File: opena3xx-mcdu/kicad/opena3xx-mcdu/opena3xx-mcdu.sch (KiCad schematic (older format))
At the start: 147 parts, among them J1 Conn_02x01, J2 Conn_02x01, J3 Conn_02x01, J4 Conn_02x01, J5 Conn_02x01, J6 Conn_02x01, J7 Conn_02x01, J8 Conn_02x01, SW1 TLL-6A, SW10 TLL-6A, SW100 SW_MEC_5E, SW11 TLL-6A, SW12 TLL-6A, SW13 TLL-6A, SW14 TLL-6A, SW15 TLL-6A, SW16 TLL-6A, SW17 TLL-6A, SW18 TLL-6A, SW19 TLL-6A, SW2 TLL-6A, SW20 TLL-6A, SW21 TLL-6A, SW22 TLL-6A, SW23 TLL-6A, SW24 TLL-6A, SW25 TLL-6A, SW26 TLL-6A, SW27 TLL-6A, SW28 TLL-6A, SW29 TLL-6A, SW3 TLL-6A, SW30 TLL-6A, SW31 TLL-6A, SW32 TLL-6A, SW33 TLL-6A, SW34 TLL-6A, SW35 TLL-6A, SW36 TLL-6A, SW37 TLL-6A, SW38 TLL-6A, SW39 TLL-6A, SW4 TLL-6A, SW40 TLL-6A, SW41 TLL-6A, SW42 TLL-6A, SW43 TLL-6A, SW44 TLL-6A, SW45 TLL-6A, SW46 TLL-6A, SW47 TLL-6A, SW48 TLL-6A, SW49 TLL-6A, SW5 TLL-6A, SW50 TLL-6A, SW51 TLL-6A, SW52 TLL-6A, SW53 TLL-6A, SW54 TLL-6A, SW55 TLL-6A, SW56 TLL-6A, SW57 TLL-6A, SW58 TLL-6A, SW59 TLL-6A, SW6 TLL-6A, SW60 TLL-6A, SW61 TLL-6A, SW62 TLL-6A, SW63 TLL-6A, SW64 TLL-6A, SW65 TLL-6A, SW66 TLL-6A, SW67 TLL-6A, SW68 TLL-6A, SW69 TLL-6A, SW7 TLL-6A, SW70 TLL-6A, SW71 TLL-6A, SW72 TLL-6A, SW73 TLL-6A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

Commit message: Added Libs + MCDU fixes + Added LCD Menu Tactile Switch
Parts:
- SW73: footprint openaa3xx:TACTILE_LED_TH -> opena3x:TACTILE_LED_TH
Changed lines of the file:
@@
 F 0 "SW73" H 18200 10830 50  0000 C CNN
 F 1 "TLL-6A" H 18200 10739 50  0000 C CNN
-F 2 "openaa3xx:TACTILE_LED_TH" H 18200 10648 50  0001 C CNN
+F 2 "opena3x:TACTILE_LED_TH" H 18200 10648 50  0001 C CNN
 F 3 "https://eu.mouser.com/datasheet/2/910/312_TL-6-1571269.pdf" H 18125 10675 50  0001 C CNN
 F 4 "DIM" H 18125 10625 50  0000 C CNN "MCDU IO Name"

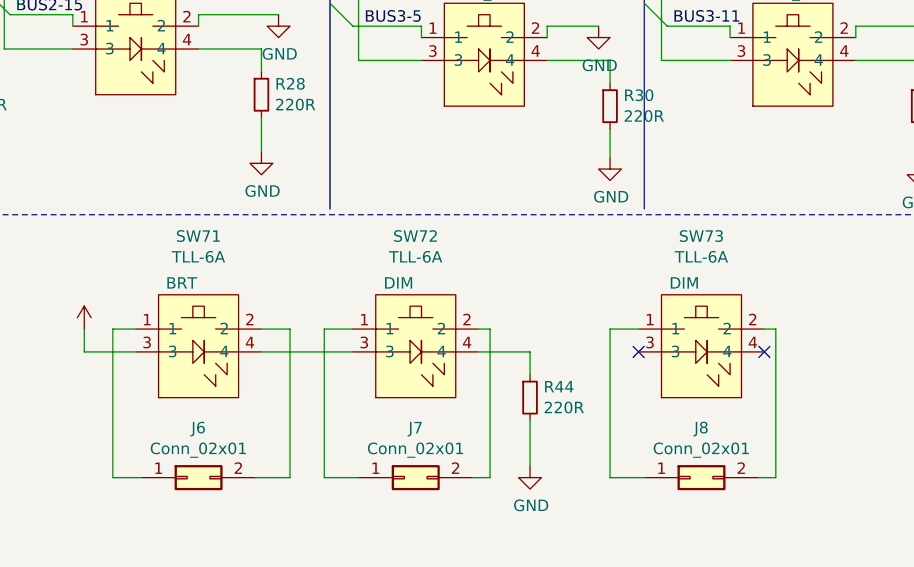
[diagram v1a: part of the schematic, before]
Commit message: Updates MCDU PCB
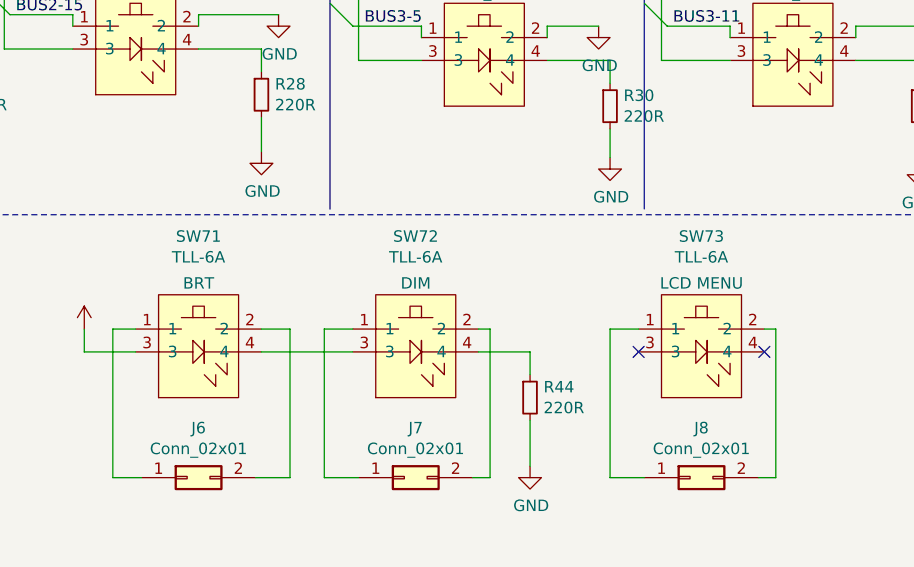
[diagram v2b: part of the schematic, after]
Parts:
- SW73: MCDU IO Name DIM -> LCD MENU
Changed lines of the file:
@@
 F 2 "openaa3xx:TACTILE_LED_TH" H 16000 10648 50  0001 C CNN
 F 3 "https://eu.mouser.com/datasheet/2/910/312_TL-6-1571269.pdf" H 15925 10675 50  0001 C CNN
-F 4 "BRT" H 15925 10625 50  0000 C CNN "MCDU IO Name"
+F 4 "BRT" H 16000 10625 50  0000 C CNN "MCDU IO Name"
 	1    15925 10625
 	1    0    0    -1
@@
 F 2 "openaa3xx:TACTILE_LED_TH" H 16950 10648 50  0001 C CNN
 F 3 "https://eu.mouser.com/datasheet/2/910/312_TL-6-1571269.pdf" H 16875 10675 50  0001 C CNN
-F 4 "DIM" H 16875 10625 50  0000 C CNN "MCDU IO Name"
+F 4 "DIM" H 16950 10625 50  0000 C CNN "MCDU IO Name"
 	1    16875 10625
 	1    0    0    -1
@@
 F 2 "opena3x:TACTILE_LED_TH" H 18200 10648 50  0001 C CNN
 F 3 "https://eu.mouser.com/datasheet/2/910/312_TL-6-1571269.pdf" H 18125 10675 50  0001 C CNN
-F 4 "DIM" H 18125 10625 50  0000 C CNN "MCDU IO Name"
+F 4 "LCD MENU" H 18200 10625 50  0000 C CNN "MCDU IO Name"
 	1    18125 10625
 	1    0    0    -1

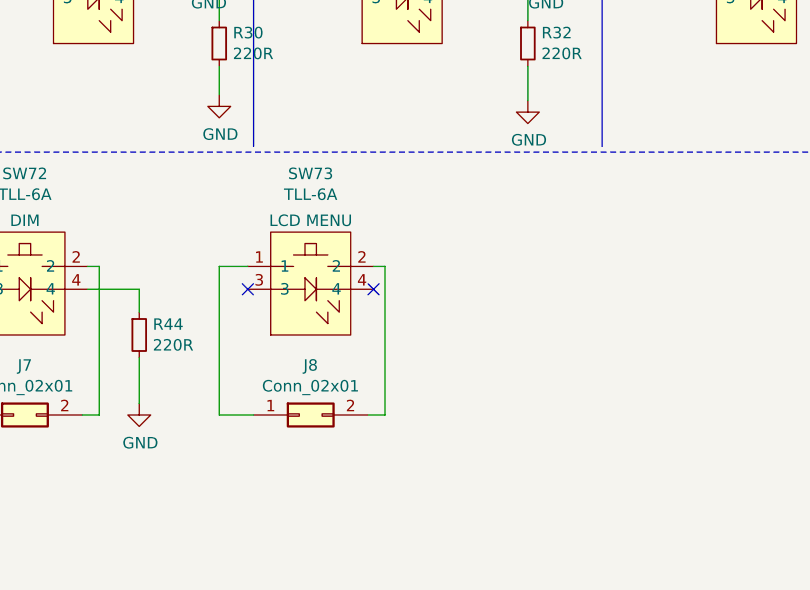
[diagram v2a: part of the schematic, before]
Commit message: MCDU Improvements Markings + Added Tactile for LCD Power + LED funcational names
MCDU Improvements Markings + Added Tactile for LCD Power + LED funcational names
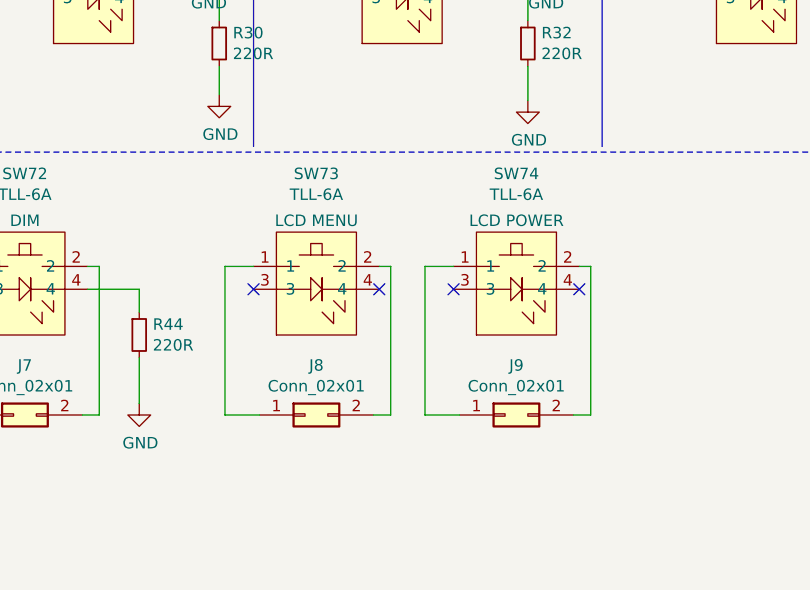
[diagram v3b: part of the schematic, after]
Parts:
- added J9: Conn_02x01, TerminalBlock:TerminalBlock_bornier-2_P5.08mm, symbol Connector_Generic:Conn_02x01
- added SW74: TLL-6A, opena3x:TACTILE_LED_TH, symbol opena3xx-mcdu-rescue:TLL-6A-opena3xx-kicad
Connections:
- new net: J9.1 (Pin_1), SW74.1
- new net: J9.2 (Pin_2), SW74.2
- no-connect marks 35 -> 37
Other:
- moved on the sheet: J8, SW73
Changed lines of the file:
@@
 L opena3xx-mcdu-rescue:TLL-6A-opena3xx-kicad SW73
 U 1 1 60CF5AE0
-P 18125 10625
-F 0 "SW73" H 18200 10830 50  0000 C CNN
-F 1 "TLL-6A" H 18200 10739 50  0000 C CNN
-F 2 "opena3x:TACTILE_LED_TH" H 18200 10648 50  0001 C CNN
-F 3 "https://eu.mouser.com/datasheet/2/910/312_TL-6-1571269.pdf" H 18125 10675 50  0001 C CNN
-F 4 "LCD MENU" H 18200 10625 50  0000 C CNN "MCDU IO Name"
-	1    18125 10625
+P 18150 10625
+F 0 "SW73" H 18225 10830 50  0000 C CNN
+F 1 "TLL-6A" H 18225 10739 50  0000 C CNN
+F 2 "opena3x:TACTILE_LED_TH" H 18225 10648 50  0001 C CNN
+F 3 "https://eu.mouser.com/datasheet/2/910/312_TL-6-1571269.pdf" H 18150 10675 50  0001 C CNN
+F 4 "LCD MENU" H 18225 10625 50  0000 C CNN "MCDU IO Name"
+	1    18150 10625
 	1    0    0    -1
 $EndComp
@@
 L Connector_Generic:Conn_02x01 J8
 U 1 1 60CF5AF6
-P 18150 11475
-F 0 "J8" H 18200 11692 50  0000 C CNN
-F 1 "Conn_02x01" H 18200 11601 50  0000 C CNN
-F 2 "TerminalBlock:TerminalBlock_bornier-2_P5.08mm" H 18150 11475 50  0001 C CNN
-F 3 "~" H 18150 11475 50  0001 C CNN
-	1    18150 11475
+P 18175 11475
+F 0 "J8" H 18225 11692 50  0000 C CNN
+F 1 "Conn_02x01" H 18225 11601 50  0000 C CNN
+F 2 "TerminalBlock:TerminalBlock_bornier-2_P5.08mm" H 18175 11475 50  0001 C CNN
+F 3 "~" H 18175 11475 50  0001 C CNN
+	1    18175 11475
 	1    0    0    -1
 $EndComp
 Wire Wire Line
-	17800 10825 17800 11475
+	17825 10825 17825 11475
 Wire Wire Line
-	17800 11475 17950 11475
+	17825 11475 17975 11475
 Wire Wire Line
-	18450 11475 18525 11475
+	18475 11475 18550 11475
 Wire Wire Line
-	18525 11475 18525 10825
+	18550 11475 18550 10825
 Wire Wire Line
-	18525 10825 18475 10825
+	18550 10825 18500 10825
 Wire Wire Line
-	17800 10825 17925 10825
-NoConn ~ 18475 10925
-NoConn ~ 17925 10925
+	17825 10825 17950 10825
+NoConn ~ 18500 10925
+NoConn ~ 17950 10925
+$Comp
+L opena3xx-mcdu-rescue:TLL-6A-opena3xx-kicad SW74
+U 1 1 60E35CFB
+P 19025 10625
+F 0 "SW74" H 19100 10830 50  0000 C CNN
+F 1 "TLL-6A" H 19100 10739 50  0000 C CNN
+F 2 "opena3x:TACTILE_LED_TH" H 19100 10648 50  0001 C CNN
+F 3 "https://eu.mouser.com/datasheet/2/910/312_TL-6-1571269.pdf" H 19025 10675 50  0001 C CNN
+F 4 "LCD POWER" H 19100 10625 50  0000 C CNN "MCDU IO Name"
+	1    19025 10625
+	1    0    0    -1
+$EndComp
+$Comp
+L Connector_Generic:Conn_02x01 J9
+U 1 1 60E35D01
+P 19050 11475
+F 0 "J9" H 19100 11692 50  0000 C CNN
+F 1 "Conn_02x01" H 19100 11601 50  0000 C CNN
+F 2 "TerminalBlock:TerminalBlock_bornier-2_P5.08mm" H 19050 11475 50  0001 C CNN
+F 3 "~" H 19050 11475 50  0001 C CNN
+	1    19050 11475
+	1    0    0    -1
+$EndComp
+Wire Wire Line
+	18700 10825 18700 11475
+Wire Wire Line
+	18700 11475 18850 11475
+Wire Wire Line
+	19350 11475 19425 11475
+Wire Wire Line
+	19425 11475 19425 10825
+Wire Wire Line
+	19425 10825 19375 10825
+Wire Wire Line
+	18700 10825 18825 10825
+NoConn ~ 19375 10925
+NoConn ~ 18825 10925
 Wire Bus Line
 	20850 5125 20850 10300

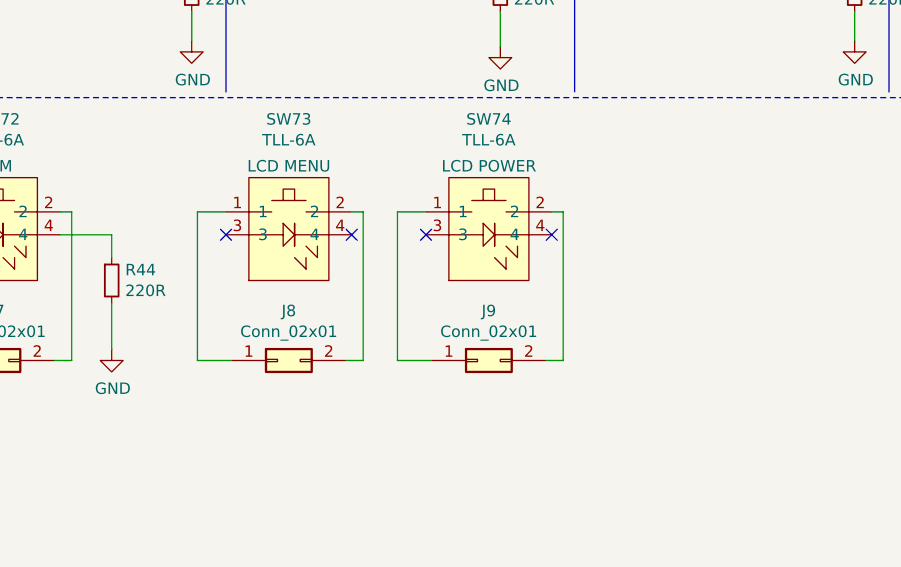
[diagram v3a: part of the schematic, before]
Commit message: PCB Update
1) 12V connecters moved up slightly to allow room for mounting nut.
2) Connected the LED's for the 'LCD MENU' and 'LCD PWR'.
3) Added 2 resistors for the 'LCD MENU' and 'LCD PWR' to allow direct connection to the display PCB.
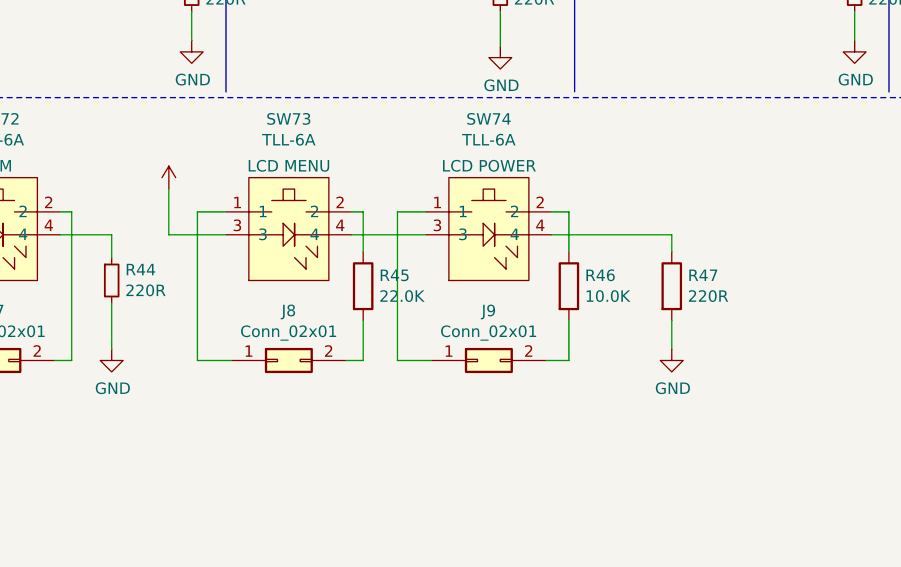
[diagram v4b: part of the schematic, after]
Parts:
- added R45: 22.0K, Resistor_SMD:R_1210_3225Metric_Pad1.30x2.65mm_HandSolder, symbol Device:R
- added R46: 10.0K, Resistor_SMD:R_1210_3225Metric_Pad1.30x2.65mm_HandSolder, symbol Device:R
- added R47: 220R, Resistor_SMD:R_1210_3225Metric_Pad1.30x2.65mm_HandSolder, symbol Device:R
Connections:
- net +12V: now also SW73.3
- net GND: now also R47.2
- net at SW73.2: now also R45.1; no longer J8.2 (Pin_2)
- net at SW73.4: now also SW74.3
- net at SW74.2: now also R46.1; no longer J9.2 (Pin_2)
- net at SW74.4: now also R47.1
- new net: J8.2 (Pin_2), R45.2
- new net: J9.2 (Pin_2), R46.2
- no-connect marks 37 -> 33
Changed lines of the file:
@@
 	18475 11475 18550 11475
 Wire Wire Line
-	18550 11475 18550 10825
+	18550 11475 18550 11300
 Wire Wire Line
 	18550 10825 18500 10825
 Wire Wire Line
 	17825 10825 17950 10825
-NoConn ~ 18500 10925
-NoConn ~ 17950 10925
 $Comp
 L opena3xx-mcdu-rescue:TLL-6A-opena3xx-kicad SW74
@@
 	18700 11475 18850 11475
 Wire Wire Line
-	19350 11475 19425 11475
+	18700 10825 18825 10825
+$Comp
+L Device:R R45
+U 1 1 61E2AB88
+P 18550 11150
+F 0 "R45" H 18620 11196 50  0000 L CNN
+F 1 "22.0K" H 18620 11105 50  0000 L CNN
+F 2 "Resistor_SMD:R_1210_3225Metric_Pad1.30x2.65mm_HandSolder" V 18480 11150 50  0001 C CNN
+F 3 "~" H 18550 11150 50  0001 C CNN
+	1    18550 11150
+	1    0    0    -1
+$EndComp
 Wire Wire Line
-	19425 11475 19425 10825
+	18550 11000 18550 10825
+$Comp
+L Device:R R46
+U 1 1 61E2B673
+P 19450 11150
+F 0 "R46" H 19520 11196 50  0000 L CNN
+F 1 "10.0K" H 19520 11105 50  0000 L CNN
+F 2 "Resistor_SMD:R_1210_3225Metric_Pad1.30x2.65mm_HandSolder" V 19380 11150 50  0001 C CNN
+F 3 "~" H 19450 11150 50  0001 C CNN
+	1    19450 11150
+	1    0    0    -1
+$EndComp
 Wire Wire Line
-	19425 10825 19375 10825
+	19350 11475 19450 11475
 Wire Wire Line
-	18700 10825 18825 10825
-NoConn ~ 19375 10925
-NoConn ~ 18825 10925
+	19450 11475 19450 11300
+Wire Wire Line
+	19450 10825 19450 11000
+Wire Wire Line
+	19375 10825 19450 10825
+Wire Wire Line
+	17950 10925 17700 10925
+Wire Wire Line
+	17700 10925 17700 10725
+Wire Wire Line
+	18500 10925 18825 10925
+Wire Wire Line
+	19375 10925 19900 10925
+Wire Wire Line
+	19900 10925 19900 11000
+$Comp
+L power:+12V #PWR0143
+U 1 1 62B671C7
+P 17700 10725
+F 0 "#PWR0143" H 17700 10575 50  0001 C CNN
+F 1 "+12V" H 17715 10898 50  0001 C CNN
+F 2 "" H 17700 10725 50  0001 C CNN
+F 3 "" H 17700 10725 50  0001 C CNN
+	1    17700 10725
+	1    0    0    -1
+$EndComp
+$Comp
+L power:GND #PWR0145
+U 1 1 62C3D062
+P 19900 11425
+F 0 "#PWR0145" H 19900 11175 50  0001 C CNN
+F 1 "GND" H 19905 11252 50  0000 C CNN
+F 2 "" H 19900 11425 50  0001 C CNN
+F 3 "" H 19900 11425 50  0001 C CNN
+	1    19900 11425
+	1    0    0    -1
+$EndComp
 Wire Bus Line
 	20850 5125 20850 10300
@@
 Wire Bus Line
 	8050 2025 8050 3725
+$Comp
+L Device:R R47
+U 1 1 62D12A23
+P 19900 11150
+F 0 "R47" H 19970 11196 50  0000 L CNN
+F 1 "220R" H 19970 11105 50  0000 L CNN
+F 2 "Resistor_SMD:R_1210_3225Metric_Pad1.30x2.65mm_HandSolder" V 19830 11150 50  0001 C CNN
+F 3 "~" H 19900 11150 50  0001 C CNN
+	1    19900 11150
+	1    0    0    -1
+$EndComp
+Wire Wire Line
+	19900 11300 19900 11425
 $EndSCHEMATC
